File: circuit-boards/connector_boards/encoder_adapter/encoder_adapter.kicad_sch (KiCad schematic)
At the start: 4 parts, among them J1 Encoder, J2 Conn_01x05_Male

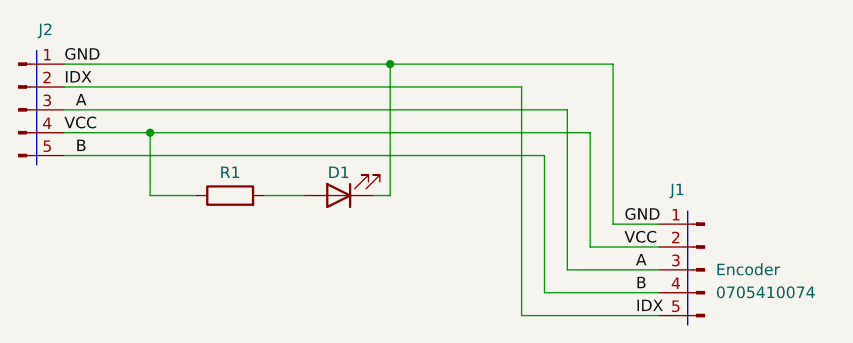
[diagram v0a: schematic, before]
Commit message: Updated boms and exported output files for connector boards
Signed-off-by: Scott <sgberman1@gmail.com>
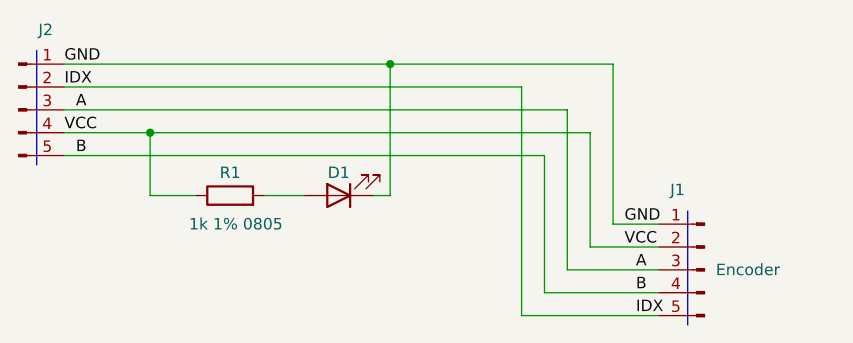
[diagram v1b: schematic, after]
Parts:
- D1: DIST (none) -> Digikey; DIST P/N (none) -> 1080-1419-1-ND; MFG (none) -> Everlight Electronics Co Ltd
- J1: DIST (none) -> Digikey; DIST P/N (none) -> WM20416-ND
- J2: now left out of the parts list
- R1: value R -> 1k 1% 0805; DIST (none) -> Digikey; DIST P/N (none) -> 311-1.00KCRCT-ND; MFG (none) -> YAGEO; MFG P/N (none) -> RC0805FR-071KL
